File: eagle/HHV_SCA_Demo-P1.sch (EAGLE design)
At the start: 35 parts, among them CN1 MINIUSB-SMD, CN3 CON, U1 PIC12F1572, U2 FT230XS, U3 AOZ8105CI

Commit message: eagle: Final draft of P1 rev
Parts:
- removed FB2: (no value), rcl:R-EU_R0603
- renumbered LED1 to D1, LED2 to D2, LED3 to D3, LED4 to D4
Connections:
- removed net ICSPDAT: CN3.4
- removed net N$10: C3.1
- removed net N$7: CN1.GND, FB2.2
- removed net N$9: C3.2
- net FTDI_RXD: now also CN3.4
- net USB_5V: now also C3.1
- net USB_DM: now also U3.IO1@1; no longer U3.IO4@6
- net USB_DP: now also U3.IO2@3; no longer U3.IO1@1
- net VSS: now also C3.2, CN1.GND; no longer FB2.1
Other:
- note added: "PICkit 3"
- note removed: "Verify!"

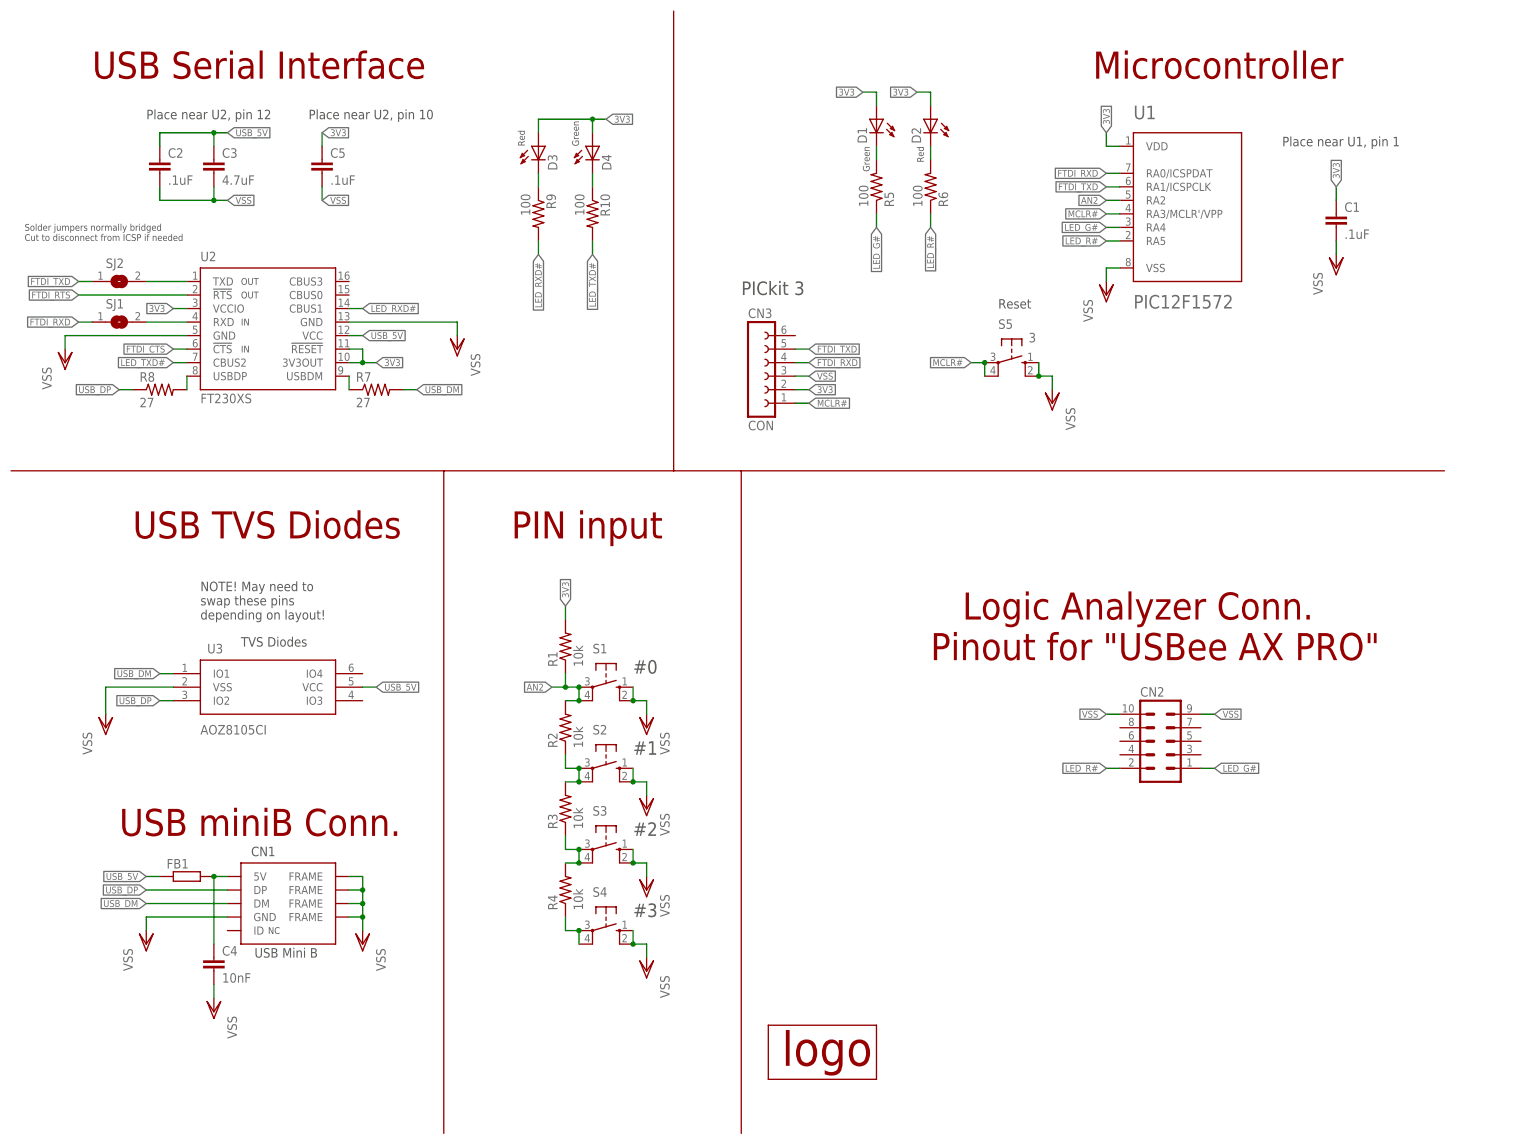
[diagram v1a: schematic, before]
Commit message: eagle: Finalized schematic and board files
Added donation text to back silkscreen
Changed schematic names of S* to SW*
Removed value from SW5
Added color values to D*
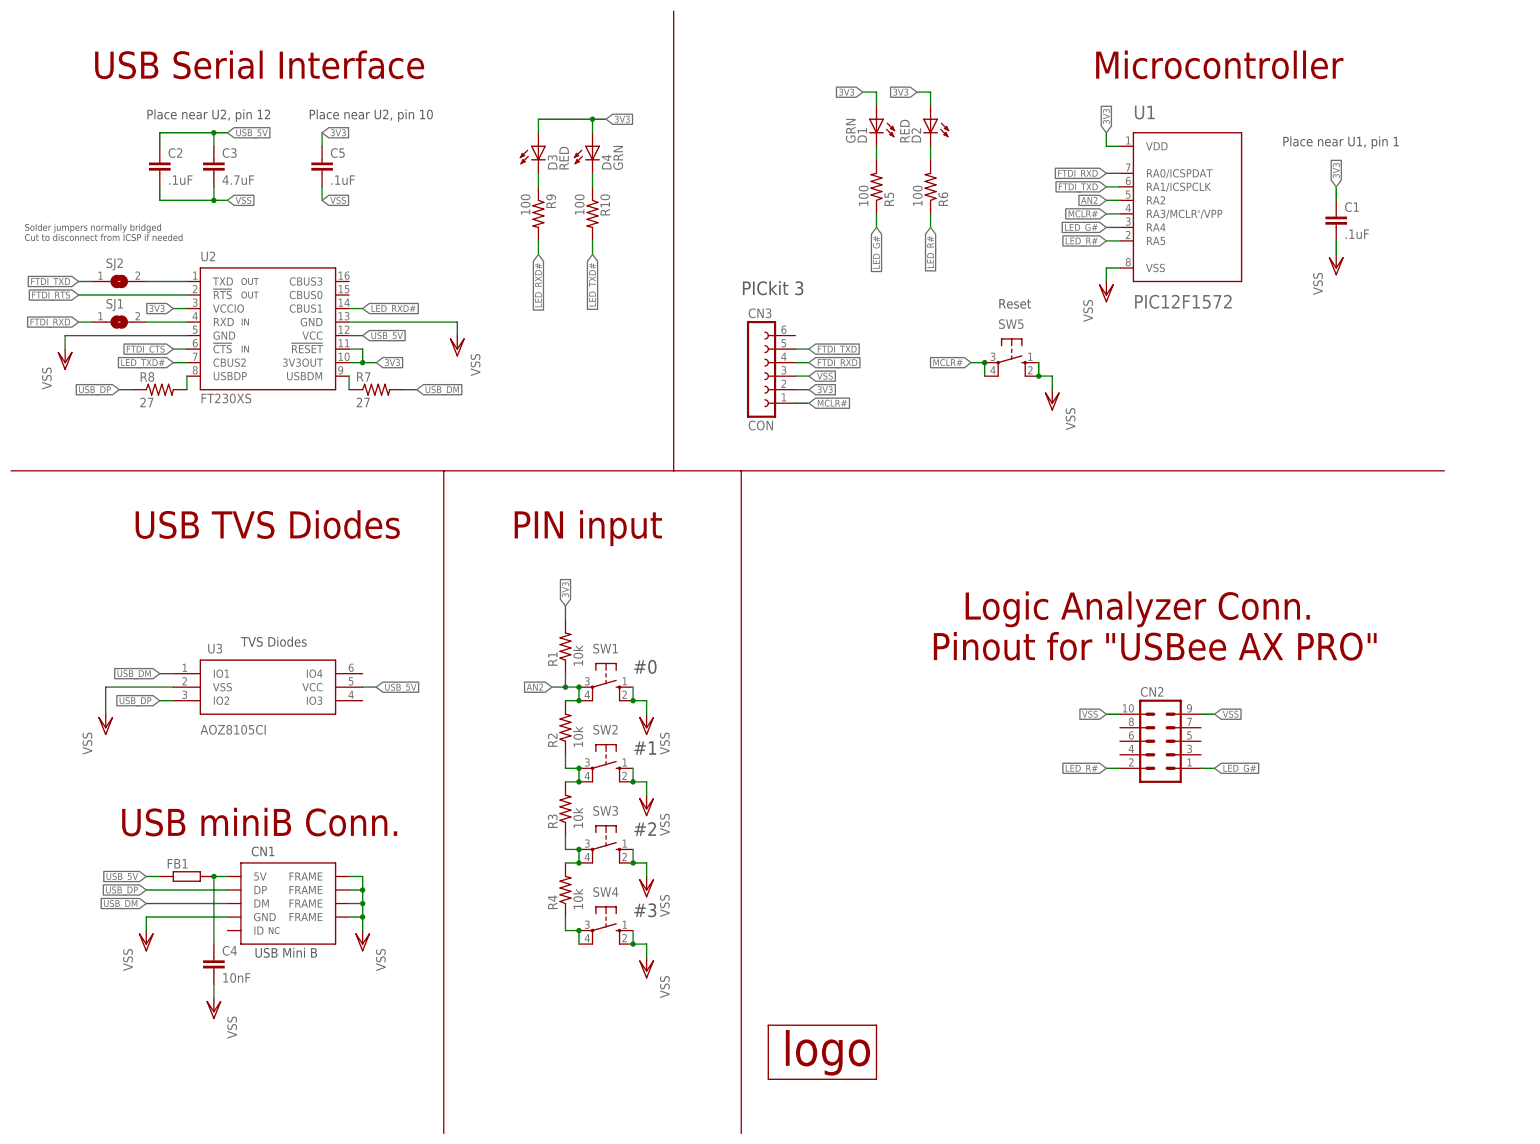
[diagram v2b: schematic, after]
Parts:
- D1, D4: value (none) -> GRN
- D2, D3: value (none) -> RED
- SW5: value 3 -> (none)
- renumbered S1 to SW1, S2 to SW2, S3 to SW3, S4 to SW4, S5 to SW5
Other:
- note removed: "Green"
- note removed: "NOTE! May need to swap these pins depending on layout!"
- note removed: "Red"
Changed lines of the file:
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@@
 <part name="VSS2" library="supply1" deviceset="VSS" device=""/>
 <part name="CN3" library="con-lsta" deviceset="FE06-1" device="" value="CON"/>
-<part name="S1" library="switch-omron" deviceset="10-XX" device=""/>
-<part name="S2" library="switch-omron" deviceset="10-XX" device=""/>
-<part name="S3" library="switch-omron" deviceset="10-XX" device=""/>
-<part name="S4" library="switch-omron" deviceset="10-XX" device=""/>
+<part name="SW1" library="switch-omron" deviceset="10-XX" device=""/>
+<part name="SW2" library="switch-omron" deviceset="10-XX" device=""/>
+<part name="SW3" library="switch-omron" deviceset="10-XX" device=""/>
+<part name="SW4" library="switch-omron" deviceset="10-XX" device=""/>
 <part name="R2" library="rcl" deviceset="R-US_" device="R0603" value="10k"/>
 <part name="R3" library="rcl" deviceset="R-US_" device="R0603" value="10k"/>
@@
 <part name="VSS12" library="supply1" deviceset="VSS" device=""/>
 <part name="C5" library="rcl" deviceset="C-EU" device="C0603K" value=".1uF"/>
-<part name="D3" library="led" deviceset="LED" device="3MM"/>
-<part name="D4" library="led" deviceset="LED" device="3MM"/>
+<part name="D3" library="led" deviceset="LED" device="3MM" value="RED"/>
+<part name="D4" library="led" deviceset="LED" device="3MM" value="GRN"/>
 <part name="R9" library="rcl" deviceset="R-US_" device="R0603" value="100"/>
 <part name="R10" library="rcl" deviceset="R-US_" device="R0603" value="100"/>
-<part name="D1" library="led" deviceset="LED" device="3MM"/>
-<part name="D2" library="led" deviceset="LED" device="3MM"/>
+<part name="D1" library="led" deviceset="LED" device="3MM" value="GRN"/>
+<part name="D2" library="led" deviceset="LED" device="3MM" value="RED"/>
 <part name="CN2" library="con-lstb" deviceset="MA05-2" device=""/>
 <part name="U1" library="cuslibrary" deviceset="PIC12F1571" device="" value="PIC12F1572"/>
-<part name="S5" library="switch-omron" deviceset="10-XX" device="" value="3"/>
+<part name="SW5" library="switch-omron" deviceset="10-XX" device=""/>
 <part name="VSS13" library="supply1" deviceset="VSS" device=""/>
 <part name="C1" library="rcl" deviceset="C-EU" device="C0603K" value=".1uF"/>
@@
 <text x="50.165" y="52.07" size="1.778" layer="97" ratio="15">CN1</text>
 <text x="50.8" y="33.02" size="1.778" layer="97" ratio="15">USB Mini B</text>
-<text x="40.64" y="96.52" size="1.778" layer="97" ratio="15">NOTE! May need to
-swap these pins
-depending on layout!</text>
-<text x="101.6" y="185.42" size="1.27" layer="97" ratio="15" rot="R90">Red</text>
-<text x="111.76" y="185.42" size="1.27" layer="97" ratio="15" rot="R90">Green</text>
-<text x="175.26" y="185.42" size="1.27" layer="97" ratio="15" rot="R270">Red</text>
-<text x="165.1" y="185.42" size="1.27" layer="97" ratio="15" rot="R270">Green</text>
 <text x="142.24" y="157.48" size="2.54" layer="97" ratio="15">PICkit 3</text>
 <text x="243.84" y="185.42" size="1.778" layer="97" ratio="15">Place near U1, pin 1</text>
@@
 <instance part="VSS2" gate="G$1" x="254" y="162.56"/>
 <instance part="CN3" gate="G$1" x="144.78" y="142.24"/>
-<instance part="S1" gate="1" x="116.84" y="83.82" rot="R270"/>
-<instance part="S2" gate="1" x="116.84" y="68.58" rot="R270"/>
-<instance part="S3" gate="1" x="116.84" y="53.34" rot="R270"/>
-<instance part="S4" gate="1" x="116.84" y="38.1" rot="R270"/>
+<instance part="SW1" gate="1" x="116.84" y="83.82" rot="R270"/>
+<instance part="SW2" gate="1" x="116.84" y="68.58" rot="R270"/>
+<instance part="SW3" gate="1" x="116.84" y="53.34" rot="R270"/>
+<instance part="SW4" gate="1" x="116.84" y="38.1" rot="R270"/>
 <instance part="R2" gate="G$1" x="109.22" y="76.2" rot="R90"/>
 <instance part="R3" gate="G$1" x="109.22" y="60.96" rot="R90"/>
@@
 <instance part="CN2" gate="G$1" x="220.98" y="73.66"/>
 <instance part="U1" gate="G$1" x="233.68" y="167.64"/>
-<instance part="S5" gate="1" x="193.04" y="144.78" rot="R270"/>
+<instance part="SW5" gate="1" x="193.04" y="144.78" rot="R270"/>
 <instance part="VSS13" gate="G$1" x="200.66" y="137.16" rot="MR0"/>
 <instance part="C1" gate="G$1" x="254" y="172.72"/>
@@
 </segment>
 <segment>
-<pinref part="S5" gate="1" pin="P1"/>
-<pinref part="S5" gate="1" pin="P"/>
+<pinref part="SW5" gate="1" pin="P1"/>
+<pinref part="SW5" gate="1" pin="P"/>
 <wire x1="187.96" y1="142.24" x2="187.96" y2="144.78" width="0.1524" layer="91"/>
 <wire x1="187.96" y1="144.78" x2="185.42" y2="144.78" width="0.1524" layer="91"/>
@@
 </segment>
 <segment>
-<pinref part="S4" gate="1" pin="S1"/>
+<pinref part="SW4" gate="1" pin="S1"/>
 <wire x1="124.46" y1="33.02" x2="124.46" y2="35.56" width="0.1524" layer="91"/>
 <wire x1="124.46" y1="35.56" x2="121.92" y2="35.56" width="0.1524" layer="91"/>
-<pinref part="S4" gate="1" pin="S"/>
+<pinref part="SW4" gate="1" pin="S"/>
 <wire x1="121.92" y1="35.56" x2="121.92" y2="38.1" width="0.1524" layer="91"/>
 <junction x="121.92" y="35.56"/>
@@
 </segment>
 <segment>
-<pinref part="S3" gate="1" pin="S1"/>
+<pinref part="SW3" gate="1" pin="S1"/>
 <wire x1="124.46" y1="48.26" x2="124.46" y2="50.8" width="0.1524" layer="91"/>
 <wire x1="124.46" y1="50.8" x2="121.92" y2="50.8" width="0.1524" layer="91"/>
-<pinref part="S3" gate="1" pin="S"/>
+<pinref part="SW3" gate="1" pin="S"/>
 <wire x1="121.92" y1="50.8" x2="121.92" y2="53.34" width="0.1524" layer="91"/>
 <junction x="121.92" y="50.8"/>
@@
 </segment>
 <segment>
-<pinref part="S2" gate="1" pin="S1"/>
+<pinref part="SW2" gate="1" pin="S1"/>
 <wire x1="124.46" y1="63.5" x2="124.46" y2="66.04" width="0.1524" layer="91"/>
 <wire x1="124.46" y1="66.04" x2="121.92" y2="66.04" width="0.1524" layer="91"/>
-<pinref part="S2" gate="1" pin="S"/>
+<pinref part="SW2" gate="1" pin="S"/>
 <wire x1="121.92" y1="66.04" x2="121.92" y2="68.58" width="0.1524" layer="91"/>
 <junction x="121.92" y="66.04"/>
@@
 </segment>
 <segment>
-<pinref part="S1" gate="1" pin="S1"/>
+<pinref part="SW1" gate="1" pin="S1"/>
 <wire x1="124.46" y1="78.74" x2="124.46" y2="81.28" width="0.1524" layer="91"/>
 <wire x1="124.46" y1="81.28" x2="121.92" y2="81.28" width="0.1524" layer="91"/>
-<pinref part="S1" gate="1" pin="S"/>
+<pinref part="SW1" gate="1" pin="S"/>
 <wire x1="121.92" y1="81.28" x2="121.92" y2="83.82" width="0.1524" layer="91"/>
 <junction x="121.92" y="81.28"/>
@@
 </segment>
 <segment>
-<pinref part="S5" gate="1" pin="S"/>
-<pinref part="S5" gate="1" pin="S1"/>
+<pinref part="SW5" gate="1" pin="S"/>
+<pinref part="SW5" gate="1" pin="S1"/>
 <wire x1="198.12" y1="144.78" x2="198.12" y2="142.24" width="0.1524" layer="91"/>
 <wire x1="200.66" y1="142.24" x2="198.12" y2="142.24" width="0.1524" layer="91"/>
@@
 <net name="N$1" class="0">
 <segment>
-<pinref part="S4" gate="1" pin="P1"/>
-<pinref part="S4" gate="1" pin="P"/>
+<pinref part="SW4" gate="1" pin="P1"/>
+<pinref part="SW4" gate="1" pin="P"/>
 <wire x1="111.76" y1="35.56" x2="111.76" y2="38.1" width="0.1524" layer="91"/>
 <pinref part="R4" gate="G$1" pin="1"/>
@@
 <segment>
 <pinref part="R4" gate="G$1" pin="2"/>
-<pinref part="S3" gate="1" pin="P1"/>
+<pinref part="SW3" gate="1" pin="P1"/>
 <wire x1="109.22" y1="50.8" x2="111.76" y2="50.8" width="0.1524" layer="91"/>
-<pinref part="S3" gate="1" pin="P"/>
+<pinref part="SW3" gate="1" pin="P"/>
 <wire x1="111.76" y1="50.8" x2="111.76" y2="53.34" width="0.1524" layer="91"/>
 <junction x="111.76" y="50.8"/>
@@
 <segment>
 <pinref part="R3" gate="G$1" pin="2"/>
-<pinref part="S2" gate="1" pin="P1"/>
+<pinref part="SW2" gate="1" pin="P1"/>
 <wire x1="109.22" y1="66.04" x2="111.76" y2="66.04" width="0.1524" layer="91"/>
-<pinref part="S2" gate="1" pin="P"/>
+<pinref part="SW2" gate="1" pin="P"/>
 <wire x1="111.76" y1="66.04" x2="111.76" y2="68.58" width="0.1524" layer="91"/>
 <junction x="111.76" y="66.04"/>
@@
 <segment>
 <pinref part="R2" gate="G$1" pin="2"/>
-<pinref part="S1" gate="1" pin="P1"/>
+<pinref part="SW1" gate="1" pin="P1"/>
 <wire x1="109.22" y1="81.28" x2="111.76" y2="81.28" width="0.1524" layer="91"/>
-<pinref part="S1" gate="1" pin="P"/>
+<pinref part="SW1" gate="1" pin="P"/>
 <wire x1="111.76" y1="81.28" x2="111.76" y2="83.82" width="0.1524" layer="91"/>
 <junction x="111.76" y="81.28"/>
